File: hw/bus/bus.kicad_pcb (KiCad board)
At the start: 2 copper layers, 99.1 x 99.1 mm, 1179 parts, among them J1 IDE STM bus, J11 IDE STM bus, J12 IDE STM bus, J13 IDE STM bus, J14 IDE STM bus, J15 IDE STM bus, J16 IDE STM bus, J17 IDE STM bus, J2 IDE STM bus, J3 IDE STM bus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

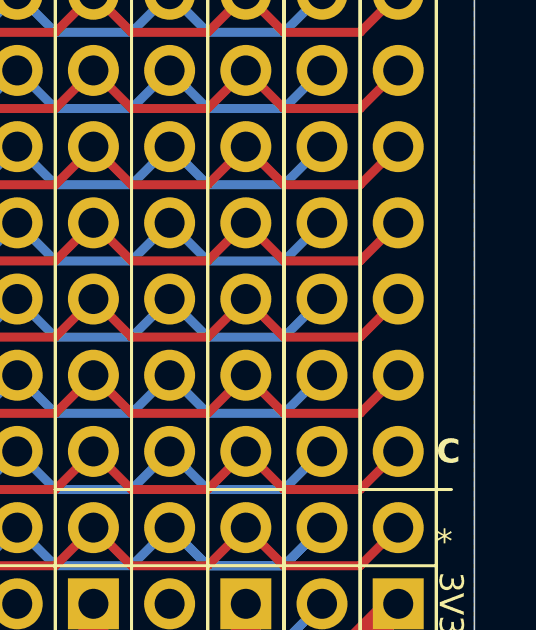
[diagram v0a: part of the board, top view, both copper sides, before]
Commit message: boot0: pullDown + serial resistor
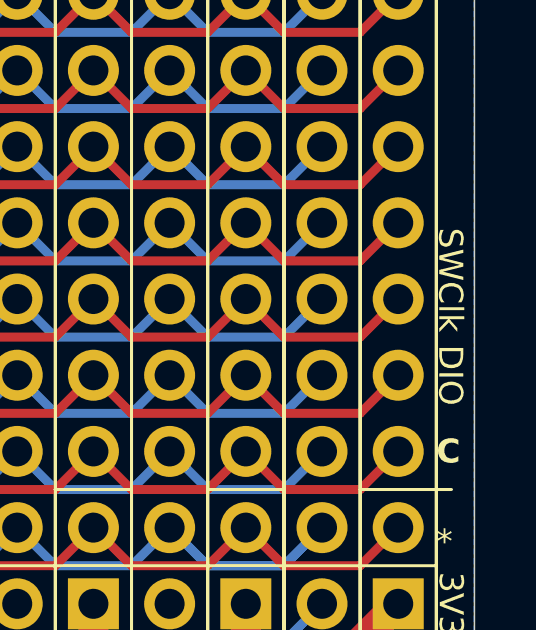
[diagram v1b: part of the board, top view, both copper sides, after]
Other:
- board text added: "DIO"
- board text added: "SWClk"
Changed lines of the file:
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@@
+		)
+	)
+	(gr_text "DIO\n"
+		(at 148.59 93.98 270)
+		(layer "F.SilkS")
+		(effects
+			(font
+				(size 0.8 0.8)
+				(thickness 0.08)
+			)
+			(justify bottom)
 		)
 	)
@@
 		(layer "F.SilkS")
 		(effects
+			(font
+				(size 0.8 0.8)
+				(thickness 0.08)
+			)
+			(justify bottom)
+		)
+	)
+	(gr_text "SWClk\n"
+		(at 148.59 90.805 270)
+		(layer "F.SilkS")
+		(effects
